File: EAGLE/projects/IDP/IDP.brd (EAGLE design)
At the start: 100 x 80 mm, 2 parts, among them M1 IDP_PROTOBOARD

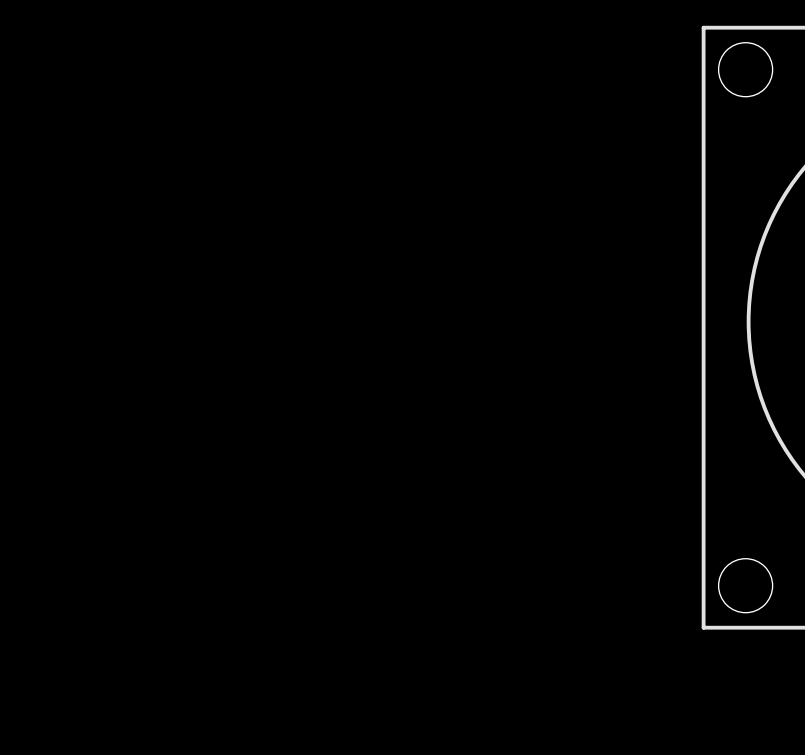
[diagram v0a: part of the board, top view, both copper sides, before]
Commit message: Added IR sensor
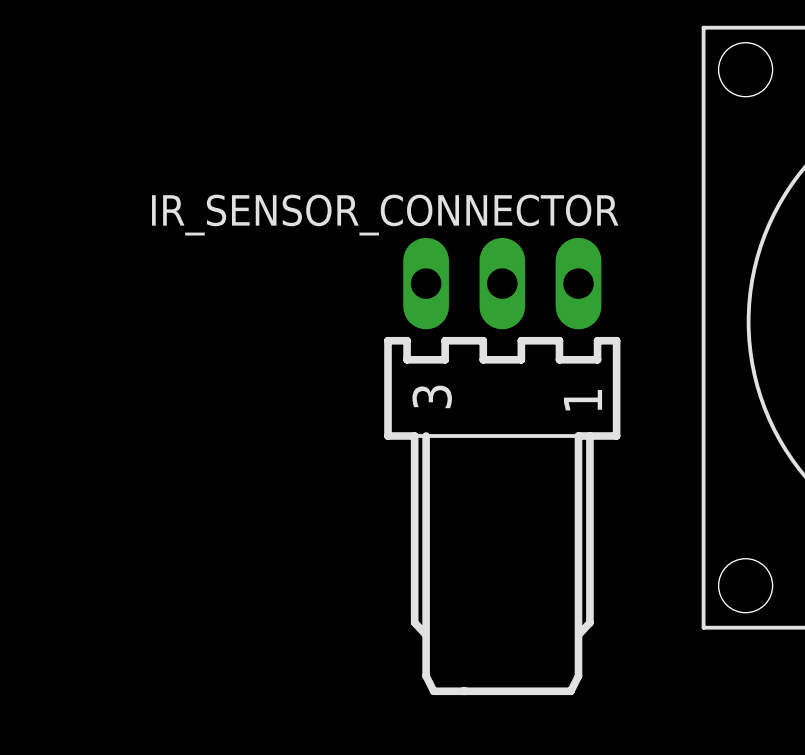
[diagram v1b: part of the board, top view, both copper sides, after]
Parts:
- added IR_SENSOR_CONNECTOR: 22-05-7038-03, IDP_library:7395-03
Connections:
- new net IR_SENSOR_VALUES: IR_SENSOR_CONNECTOR.1, M1.A2
- net +5V: now also IR_SENSOR_CONNECTOR.3
- net GND: now also IR_SENSOR_CONNECTOR.2
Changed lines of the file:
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@@
 <attribute name="VALUE" x="-59.69" y="-24.13" size="1.27" layer="27" align="top-center"/>
+</element>
+<element name="IR_SENSOR_CONNECTOR" library="IDP_library" package="7395-03" package3d_urn="urn:adsk.eagle:package:8078646/1" value="22-05-7038-03" x="-88.9" y="-11.43" smashed="yes">
+<attribute name="MF" value="MOLEX" x="-88.9" y="-11.43" size="1.778" layer="27" display="off"/>
+<attribute name="MPN" value="" x="-88.9" y="-11.43" size="1.778" layer="27" display="off"/>
+<attribute name="NAME" x="-84.9899" y="-8.4821" size="1.016" layer="25" ratio="10" rot="R180"/>
+<attribute name="OC_FARNELL" value="unknown" x="-88.9" y="-11.43" size="1.778" layer="27" display="off"/>
+<attribute name="OC_NEWARK" value="unknown" x="-88.9" y="-11.43" size="1.778" layer="27" display="off"/>
+<attribute name="POPULARITY" value="0" x="-88.9" y="-11.43" size="1.778" layer="27" display="off"/>
+<attribute name="VALUE" x="-84.2279" y="-13.8699" size="0.8128" layer="27" ratio="10" rot="R270"/>
 </element>
 </elements>
@@
 <contactref element="M1" pad="GND@48" route="any" routetag="G$1.GND"/>
 <contactref element="U$1" pad="4"/>
-<wire x1="-55.88" y1="3.81" x2="-55.88" y2="-21.59" width="0" layer="19" extent="16-16"/>
+<contactref element="IR_SENSOR_CONNECTOR" pad="2"/>
+<wire x1="-78.74" y1="3.81" x2="-88.9" y2="-11.43" width="0" layer="19" extent="16-16"/>
+<wire x1="-55.88" y1="-21.59" x2="-55.88" y2="3.81" width="0" layer="19" extent="16-16"/>
 </signal>
 <signal name="+3V3">
@@
 <contactref element="M1" pad="5V@40" route="any" routetag="G$1.5V"/>
 <contactref element="U$1" pad="1"/>
+<contactref element="IR_SENSOR_CONNECTOR" pad="3"/>
+<wire x1="-63.5" y1="-21.59" x2="-91.44" y2="-11.43" width="0" layer="19" extent="1-1"/>
 <wire x1="-43.18" y1="6.35" x2="-63.5" y2="-21.59" width="0" layer="19" extent="16-16"/>
 </signal>
@@
 <contactref element="M1" pad="A1"/>
 </signal>
+<signal name="IR_SENSOR_VALUES">
+<contactref element="M1" pad="A2"/>
+<contactref element="IR_SENSOR_CONNECTOR" pad="1"/>
+<wire x1="-25.4" y1="6.35" x2="-86.36" y2="-11.43" width="0" layer="19" extent="16-16"/>
+</signal>
 </signals>
 <mfgpreviewcolors>
@@
 </board>
 </drawing>
+<compatibility>
+<note version="8.3" severity="warning">
+Since Version 8.3, EAGLE supports URNs for individual library
+assets (packages, symbols, and devices). The URNs of those assets
+will not be understood (or retained) with this version.
+</note>
+<note version="8.3" severity="warning">
+Since Version 8.3, EAGLE supports the association of 3D packages
+with devices in libraries, schematics, and board files. Those 3D
+packages will not be understood (or retained) with this version.
+</note>
+</compatibility>
 </eagle>
